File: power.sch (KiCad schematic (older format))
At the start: 23 parts, among them J7 VIn, U7 LMR16020, U8 TPS82140

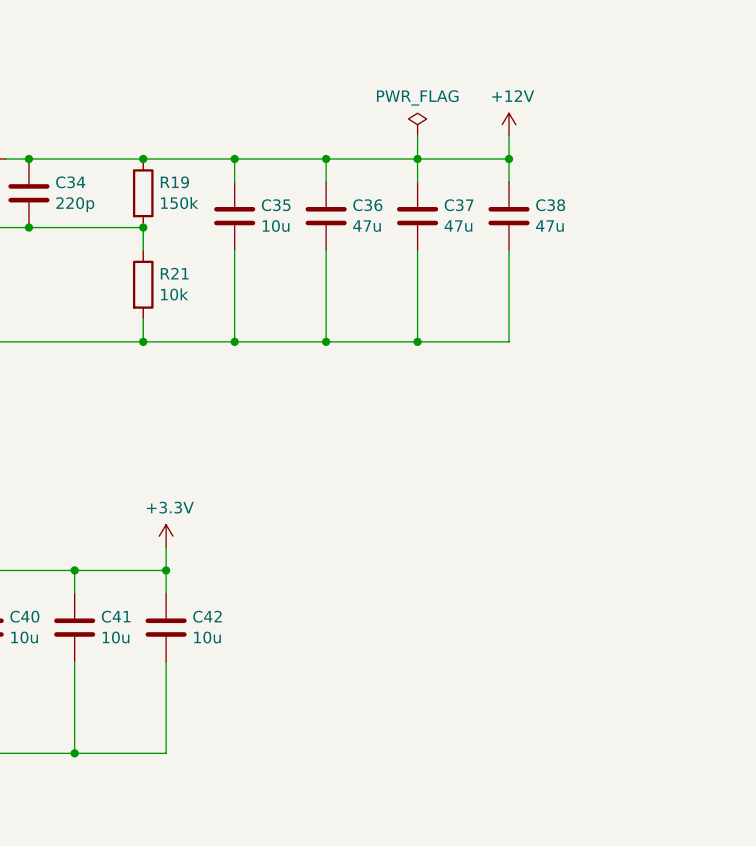
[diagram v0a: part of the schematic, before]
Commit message: Added LEDs to indicate power on the 12V and 3.3V rails Added Fiducials Moved references for SW1 and R2 Added 3D Model
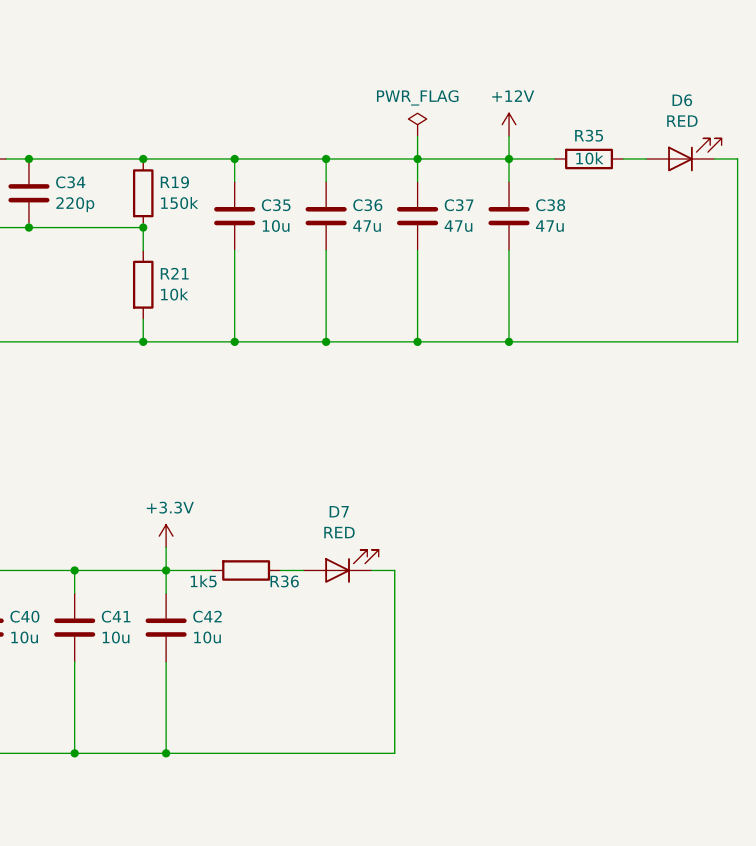
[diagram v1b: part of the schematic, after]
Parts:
- added D6, D7: RED, LED_SMD:LED_0603_1608Metric, symbol Device:LED
- added R35: 10k, Resistor_SMD:R_0603_1608Metric, symbol Device:R
- added R36: 1k5, Resistor_SMD:R_0805_2012Metric, symbol Device:R
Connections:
- net +12V: now also R35.2
- net +3V3: now also R36.2
- net GND: now also D6.1 (K), D7.1 (K)
- new net: D7.2 (A), R36.1
- new net: D6.2 (A), R35.1
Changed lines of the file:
@@
 Text Label 4700 3000 0    50   ~ 0
 B1_SW
+$Comp
+L Device:LED D?
+U 1 1 601B198E
+P 6950 4800
+AR Path="/601B198E" Ref="D?"  Part="1"
+AR Path="/5FC5F106/601B198E" Ref="D7"  Part="1"
+F 0 "D7" H 6943 4545 50  0000 C CNN
+F 1 "RED" H 6943 4636 50  0000 C CNN
+F 2 "LED_SMD:LED_0603_1608Metric" H 6950 4800 50  0001 C CNN
+F 3 "~" H 6950 4800 50  0001 C CNN
+F 4 "D-060306R1/SS2/L" H 6950 4800 50  0001 C CNN "manf#"
+F 5 "C118330" H 6950 4800 50  0001 C CNN "lcsc#"
+	1    6950 4800
+	-1   0    0    1
+$EndComp
+$Comp
+L Device:R R?
+U 1 1 601B1998
+P 6550 4800
+AR Path="/5FE0391C/601B1998" Ref="R?"  Part="1"
+AR Path="/5FE0881D/601B1998" Ref="R?"  Part="1"
+AR Path="/601B1998" Ref="R?"  Part="1"
+AR Path="/5FC5F106/601B1998" Ref="R36"  Part="1"
+F 0 "R36" V 6600 4900 50  0000 L CNN
+F 1 "1k5" V 6600 4550 50  0000 L CNN
+F 2 "Resistor_SMD:R_0805_2012Metric" V 6480 4800 50  0001 C CNN
+F 3 "~" H 6550 4800 50  0001 C CNN
+F 4 "C118217" H 6550 4800 50  0001 C CNN "lcsc#"
+F 5 "TC0525F1501T5E" H 6550 4800 50  0001 C CNN "manf#"
+	1    6550 4800
+	0    1    1    0
+$EndComp
+Wire Wire Line
+	6700 4800 6800 4800
+Wire Wire Line
+	6400 4800 6200 4800
+Wire Wire Line
+	7100 4800 7200 4800
+Wire Wire Line
+	7200 4800 7200 5600
+Wire Wire Line
+	7200 5600 6200 5600
+Connection ~ 6200 5600
+$Comp
+L Device:R R?
+U 1 1 601BDECA
+P 8050 3000
+AR Path="/5FE0391C/601BDECA" Ref="R?"  Part="1"
+AR Path="/601BDECA" Ref="R?"  Part="1"
+AR Path="/5FC5F106/601BDECA" Ref="R35"  Part="1"
+F 0 "R35" V 7950 3000 50  0000 C CNN
+F 1 "10k" V 8050 3000 50  0000 C CNN
+F 2 "Resistor_SMD:R_0603_1608Metric" V 7980 3000 50  0001 C CNN
+F 3 "~" H 8050 3000 50  0001 C CNN
+F 4 "C128781" H 8050 3000 50  0001 C CNN "lcsc#"
+F 5 "TC0325F1002T5E" H 8050 3000 50  0001 C CNN "manf#"
+	1    8050 3000
+	0    1    1    0
+$EndComp
+$Comp
+L Device:LED D?
+U 1 1 601C07BA
+P 8450 3000
+AR Path="/601C07BA" Ref="D?"  Part="1"
+AR Path="/5FC5F106/601C07BA" Ref="D6"  Part="1"
+F 0 "D6" H 8443 2745 50  0000 C CNN
+F 1 "RED" H 8443 2836 50  0000 C CNN
+F 2 "LED_SMD:LED_0603_1608Metric" H 8450 3000 50  0001 C CNN
+F 3 "~" H 8450 3000 50  0001 C CNN
+F 4 "D-060306R1/SS2/L" H 8450 3000 50  0001 C CNN "manf#"
+F 5 "C118330" H 8450 3000 50  0001 C CNN "lcsc#"
+	1    8450 3000
+	-1   0    0    1
+$EndComp
+Wire Wire Line
+	8200 3000 8300 3000
+Wire Wire Line
+	8600 3000 8700 3000
+Wire Wire Line
+	7900 3000 7700 3000
+Wire Wire Line
+	8700 3000 8700 3800
+Wire Wire Line
+	8700 3800 7700 3800
+Connection ~ 7700 3800
 $EndSCHEMATC
